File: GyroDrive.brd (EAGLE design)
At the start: 10.7 x 19.8 mm, 42 parts, among them IC1 AD8235, IC2 AD8235, IC3 AD8235, IC4 AD8235

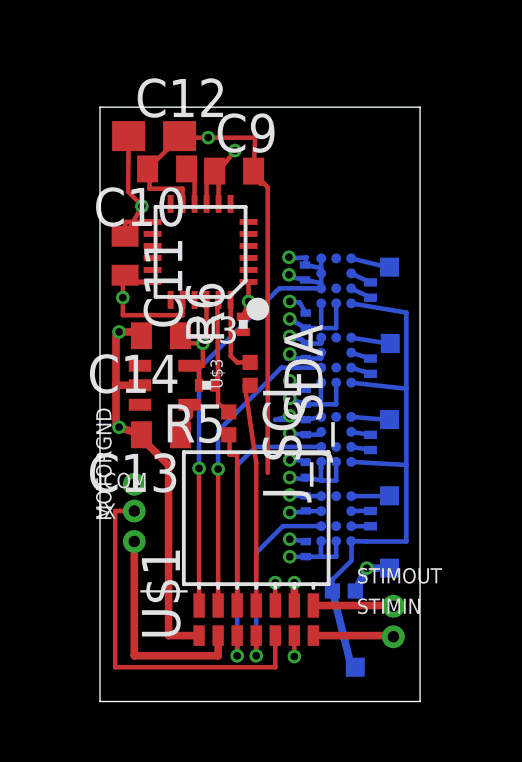
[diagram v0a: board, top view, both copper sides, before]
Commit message: Cleaned up routing around in-amps
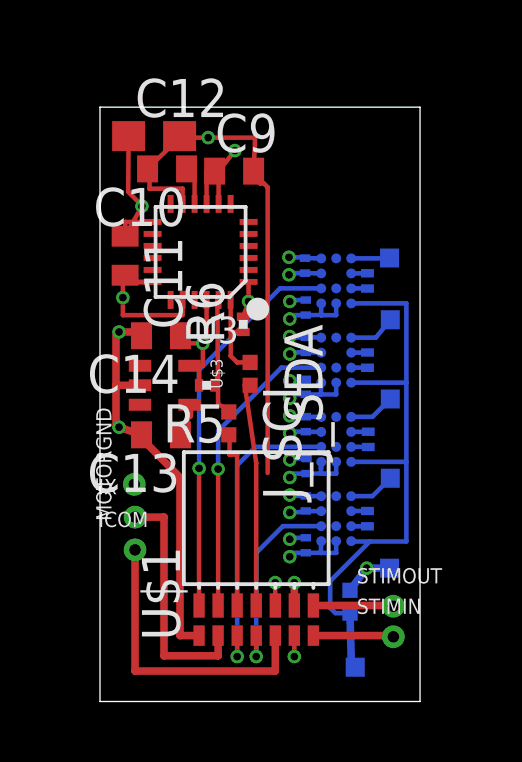
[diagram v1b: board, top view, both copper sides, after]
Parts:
- moved ICOM 1.30 mm to (1.17, 5.05)
- moved IX 0.81 mm to (1.17, 6.15)
- moved E2 0.79 mm to (9.68, 12.7)
- moved E3 0.69 mm to (9.68, 10.1)
- moved E4 0.58 mm to (9.68, 7.44)
- moved C15 0.43 mm to (6.86, 13.1)
- moved J_VGND 0.41 mm to (8.33, 3.33), turned to 90 degrees
- moved C17 0.33 mm to (6.86, 10.5)
- moved R7 0.32 mm to (8.92, 14.0)
- moved E1 0.30 mm to (9.65, 14.8)
- moved C16 0.23 mm to (6.83, 14.5)
- moved R8 0.23 mm to (8.92, 11.4)
- moved C18 0.20 mm to (6.86, 11.9)
- moved C19 0.13 mm to (6.88, 7.85)
- moved R9 0.13 mm to (8.94, 8.74)
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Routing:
- net ICOM: track 12.2 -> 9.89 mm
- net +VS: track 14.1 -> 12.2 mm
- net -VS: track 13.4 -> 11.7 mm
- net VGND: track 19.7 -> 20.7 mm
- net AGND: track 10.6 -> 9.61 mm
- net IX: track 7.28 -> 8.06 mm

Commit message: Switched +VS and -VS on pinout and analog power layer. Finished routing!
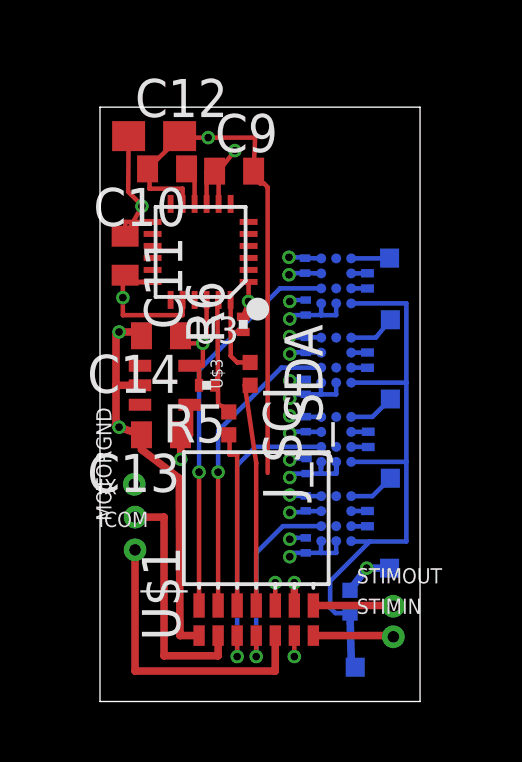
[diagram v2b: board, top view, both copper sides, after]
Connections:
- net +VS: now also U$1.T; no longer U$1.U
- net -VS: now also U$1.U; no longer U$1.T
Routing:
- net +VS: track 12.2 -> 27.2 mm, vias 5 -> 6
- net -VS: track 11.7 -> 5.64 mm
- added copper zone on layer 2, net -VS
- removed copper zone on layer 2, net +VS
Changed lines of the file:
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@@
 <wire x1="6.8152" y1="14.7788" x2="7.374" y2="14.7708" width="0.1524" layer="16"/>
 <wire x1="6.8834" y1="14.8042" x2="6.2992" y2="14.8082" width="0.1524" layer="16"/>
-<contactref element="U$1" pad="T"/>
-<wire x1="5.842" y1="3.2004" x2="5.842" y2="3.9624" width="0.1524" layer="1"/>
-<via x="5.842" y="3.9624" extent="1-16" drill="0.254"/>
-<wire x1="5.842" y1="3.9624" x2="5.842" y2="6.8834" width="0.1524" layer="2"/>
-<wire x1="5.842" y1="6.8834" x2="5.842" y2="9.398" width="0.1524" layer="2"/>
-<wire x1="5.842" y1="9.398" x2="6.3246" y2="9.525" width="0.1524" layer="2"/>
 <wire x1="6.858" y1="6.854" x2="6.354" y2="6.854" width="0.1524" layer="16"/>
 <wire x1="6.354" y1="6.854" x2="6.3246" y2="6.8834" width="0.1524" layer="16"/>
 <via x="6.3246" y="6.8834" extent="1-16" drill="0.254"/>
-<wire x1="6.3246" y1="6.8834" x2="5.842" y2="6.8834" width="0.1524" layer="2"/>
 <wire x1="7.374" y1="9.4876" x2="6.866" y2="9.4876" width="0.1524" layer="16"/>
 <wire x1="6.866" y1="9.4876" x2="6.858" y2="9.4956" width="0.1524" layer="16"/>
 <wire x1="6.858" y1="9.4956" x2="6.354" y2="9.4956" width="0.1524" layer="16"/>
 <wire x1="6.354" y1="9.4956" x2="6.3246" y2="9.525" width="0.1524" layer="16"/>
-<wire x1="7.374" y1="12.1372" x2="7.374" y2="14.7708" width="0" layer="19" extent="16-16"/>
-<wire x1="6.3246" y1="9.525" x2="6.3286" y2="12.1412" width="0" layer="19" extent="16-16"/>
-</signal>
-<signal name="+VS">
 <contactref element="U$1" pad="U"/>
+<wire x1="6.477" y1="3.2004" x2="6.477" y2="3.9624" width="0.254" layer="1"/>
+<via x="6.477" y="3.9624" extent="1-16" drill="0.254"/>
+<wire x1="6.477" y1="3.9624" x2="6.477" y2="4.318" width="0.254" layer="2"/>
 <polygon width="0.1524" layer="2">
 <vertex x="6.223" y="0"/>
 <vertex x="10.541" y="0"/>
-<vertex x="10.541" y="12.954"/>
-<vertex x="6.096" y="13.208"/>
+<vertex x="10.668" y="15.4178"/>
+<vertex x="6.0198" y="15.3924"/>
 </polygon>
+</signal>
+<signal name="+VS">
 <contactref element="U$3" pad="4"/>
 <contactref element="C13" pad="1"/>
-<wire x1="2.984" y1="9.891" x2="2.984" y2="9.525" width="0.254" layer="1"/>
-<wire x1="2.984" y1="9.525" x2="2.682" y2="8.89" width="0.1524" layer="1"/>
 <contactref element="IC1" pad="A1"/>
 <contactref element="IC2" pad="A1"/>
@@
 <wire x1="7.366" y1="5.346" x2="7.374" y2="5.346" width="0.1524" layer="16"/>
 <wire x1="7.874" y1="7.9876" x2="7.874" y2="7.5946" width="0.1524" layer="16"/>
-<wire x1="7.874" y1="7.5946" x2="7.366" y2="7.5946" width="0.1524" layer="16"/>
-<wire x1="7.366" y1="7.5946" x2="7.366" y2="7.759" width="0.1524" layer="16"/>
 <wire x1="7.366" y1="7.759" x2="7.374" y2="7.9876" width="0.1524" layer="16"/>
 <wire x1="7.366" y1="7.759" x2="7.366" y2="7.87" width="0.1524" layer="16"/>
@@
 <wire x1="6.858" y1="12.8818" x2="7.374" y2="12.8818" width="0.1524" layer="16"/>
 <wire x1="7.374" y1="12.8818" x2="7.374" y2="12.8778" width="0.1524" layer="16"/>
-<wire x1="6.8834" y1="7.5986" x2="6.3206" y2="7.5946" width="0.1524" layer="16"/>
-<wire x1="6.3206" y1="7.5946" x2="6.3246" y2="7.4676" width="0.1524" layer="16"/>
 <via x="6.3246" y="7.4676" extent="1-16" drill="0.254"/>
 <wire x1="7.366" y1="7.5946" x2="7.362" y2="7.5986" width="0.1524" layer="16"/>
-<wire x1="7.362" y1="7.5986" x2="6.8834" y2="7.5986" width="0.1524" layer="16"/>
 <wire x1="6.858" y1="4.957" x2="6.3206" y2="4.953" width="0.1524" layer="16"/>
 <wire x1="6.3206" y1="4.953" x2="6.3246" y2="4.826" width="0.1524" layer="16"/>
@@
 <wire x1="7.366" y1="4.953" x2="7.3874" y2="4.957" width="0.1524" layer="16"/>
 <wire x1="7.3874" y1="4.957" x2="6.858" y2="4.957" width="0.1524" layer="16"/>
-<wire x1="6.477" y1="3.2004" x2="6.477" y2="3.9624" width="0.254" layer="1"/>
-<via x="6.477" y="3.9624" extent="1-16" drill="0.254"/>
-<wire x1="6.477" y1="3.9624" x2="6.477" y2="4.318" width="0.254" layer="2"/>
-<wire x1="6.3246" y1="10.1092" x2="2.984" y2="9.891" width="0" layer="19" extent="1-16"/>
+<contactref element="U$1" pad="T"/>
+<wire x1="5.842" y1="3.2004" x2="5.842" y2="3.9624" width="0.1524" layer="1"/>
+<via x="5.842" y="3.9624" extent="1-16" drill="0.254"/>
+<wire x1="5.842" y1="3.9624" x2="5.842" y2="4.826" width="0.1524" layer="2"/>
+<wire x1="5.842" y1="4.826" x2="5.842" y2="7.4676" width="0.1524" layer="2"/>
+<wire x1="5.842" y1="7.4676" x2="5.842" y2="8.0772" width="0.1524" layer="2"/>
+<wire x1="5.842" y1="8.0772" x2="5.842" y2="10.1092" width="0.1524" layer="2"/>
+<wire x1="5.842" y1="10.1092" x2="5.842" y2="12.7508" width="0.1524" layer="2"/>
+<wire x1="5.842" y1="12.7508" x2="6.3246" y2="12.7508" width="0.1524" layer="2"/>
+<wire x1="6.3246" y1="4.826" x2="5.842" y2="4.826" width="0.1524" layer="2"/>
+<wire x1="6.3246" y1="10.1092" x2="5.842" y2="10.1092" width="0.1524" layer="2"/>
+<wire x1="6.3246" y1="7.4676" x2="5.842" y2="7.4676" width="0.1524" layer="2"/>
+<wire x1="7.874" y1="7.9876" x2="7.874" y2="7.5986" width="0.1524" layer="16"/>
+<wire x1="7.874" y1="7.5986" x2="7.366" y2="7.5986" width="0.1524" layer="16"/>
+<wire x1="7.366" y1="7.759" x2="7.366" y2="7.5986" width="0.1524" layer="16"/>
+<wire x1="7.362" y1="7.5986" x2="6.8834" y2="7.5986" width="0.1524" layer="16"/>
+<wire x1="6.8834" y1="7.5986" x2="6.3246" y2="7.5986" width="0.1524" layer="16"/>
+<wire x1="6.3246" y1="7.5986" x2="6.3246" y2="7.4676" width="0.1524" layer="16"/>
+<wire x1="2.682" y1="8.89" x2="2.6924" y2="8.89" width="0.1524" layer="1"/>
+<wire x1="2.6924" y1="8.89" x2="2.6924" y2="8.0772" width="0.254" layer="1"/>
+<via x="2.6924" y="8.0772" extent="1-16" drill="0.254"/>
+<wire x1="2.6924" y1="8.0772" x2="5.842" y2="8.0772" width="0.1524" layer="2"/>
+<wire x1="2.984" y1="9.891" x2="2.984" y2="8.89" width="0.254" layer="1"/>
+<wire x1="2.984" y1="8.89" x2="2.682" y2="8.89" width="0.254" layer="1"/>
+<wire x1="7.366" y1="7.5986" x2="7.362" y2="7.5986" width="0.1524" layer="16"/>
 </signal>
 <signal name="AGND">
@@
 <contactref element="IC1" pad="B1"/>
 <contactref element="U$1" pad="E"/>
-<wire x1="3.302" y1="3.2004" x2="3.302" y2="7.7724" width="0.1524" layer="1"/>
+<wire x1="3.302" y1="3.2004" x2="3.302" y2="7.6454" width="0.1524" layer="1"/>
 <wire x1="7.374" y1="13.7708" x2="5.9984" y2="13.7708" width="0.1524" layer="16"/>
-<via x="3.302" y="7.7724" extent="1-16" drill="0.254"/>
-<wire x1="3.302" y1="7.7724" x2="3.302" y2="11.049" width="0.1524" layer="16"/>
+<via x="3.302" y="7.6454" extent="1-16" drill="0.254"/>
+<wire x1="3.302" y1="7.6454" x2="3.302" y2="11.049" width="0.1524" layer="16"/>
 <wire x1="3.302" y1="11.049" x2="5.9984" y2="13.7708" width="0.1524" layer="16"/>
 </signal>
@@
 <wire x1="7.374" y1="11.1292" x2="6.0492" y2="11.1292" width="0.1524" layer="16"/>
 <wire x1="6.0492" y1="11.1292" x2="3.937" y2="9.017" width="0.1524" layer="16"/>
-<wire x1="3.937" y1="9.017" x2="3.937" y2="7.747" width="0.1524" layer="16"/>
-<via x="3.937" y="7.747" extent="1-16" drill="0.254"/>
-<wire x1="3.937" y1="7.747" x2="3.937" y2="3.2004" width="0.1524" layer="1"/>
+<wire x1="3.937" y1="9.017" x2="3.937" y2="7.6454" width="0.1524" layer="16"/>
+<via x="3.937" y="7.6454" extent="1-16" drill="0.254"/>
+<wire x1="3.937" y1="7.6454" x2="3.937" y2="3.2004" width="0.1524" layer="1"/>
 </signal>
 <signal name="VGND">
@@
 <polygon width="0.1524" layer="2">
 <vertex x="0" y="19.812"/>
-<vertex x="0" y="8.382"/>
-<vertex x="5.588" y="8.382"/>
+<vertex x="0" y="-0.0254"/>
+<vertex x="5.7404" y="0"/>
 <vertex x="5.588" y="19.812"/>
 </polygon>
@@
 <contactref element="U$1" pad="A"/>
 <wire x1="3.302" y1="2.1971" x2="2.667" y2="2.1971" width="0.254" layer="1"/>
-<wire x1="2.667" y1="2.1971" x2="2.667" y2="7.4676" width="0.254" layer="1"/>
-<wire x1="2.667" y1="7.4676" x2="1.382" y2="8.778" width="0.254" layer="1"/>
-<wire x1="1.382" y1="8.778" x2="1.382" y2="8.89" width="0.254" layer="1"/>
+<wire x1="2.667" y1="2.1971" x2="2.6416" y2="7.4422" width="0.254" layer="1"/>
+<wire x1="2.6416" y1="7.4422" x2="1.382" y2="8.397" width="0.254" layer="1"/>
+<wire x1="1.382" y1="8.397" x2="1.382" y2="8.89" width="0.254" layer="1"/>
 </signal>
 <signal name="SDA">

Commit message: Added bypass capacitor for SDA pull-up resistor, shorted SDA and SCL jumpers with traces
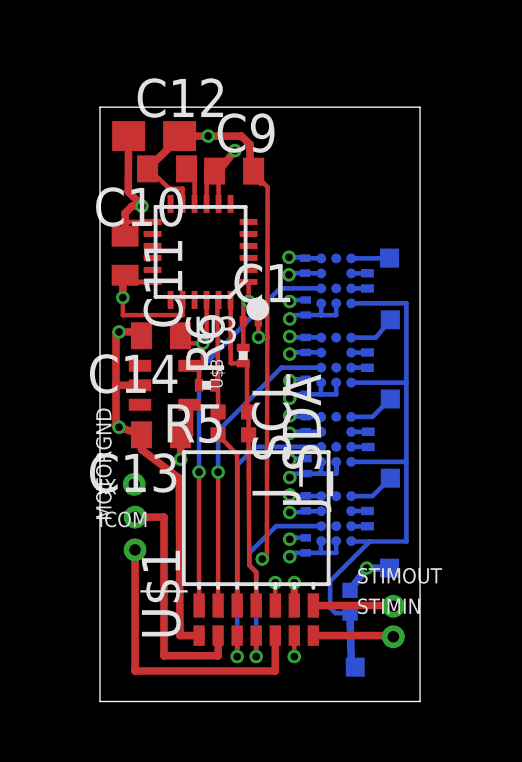
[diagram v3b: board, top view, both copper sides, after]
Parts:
- added C1: (no value), resistor:C0201
- moved J_SDA 1.65 mm to (4.95, 9.27)
- moved R6 1.04 mm to (4.78, 11.5)
- moved J_SCL 0.36 mm to (3.94, 9.27)
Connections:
- net DGND: now also C1.2
- net VDD: now also C1.1
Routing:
- net DGND: track 38.1 -> 42.7 mm, vias 4 -> 6
- net SDAOUT: track 7.55 -> 5.78 mm
- net VDD: track 26.2 -> 27.6 mm
- net SDA: track 3.02 -> 4.43 mm

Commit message: Changed pinout to group digital signals closer together
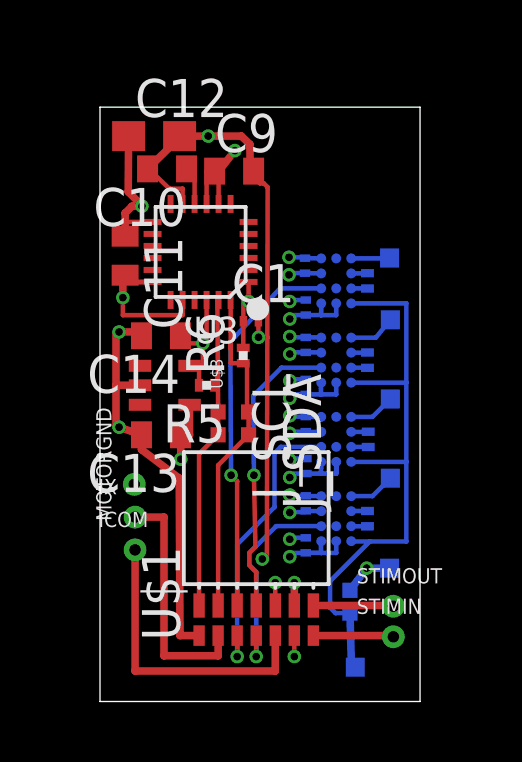
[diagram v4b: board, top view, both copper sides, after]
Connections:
- net S1: now also U$1.R; no longer U$1.E
- net S2: now also U$1.L; no longer U$1.N
- net SCLOUT: now also U$1.E; no longer U$1.R
- net SDAOUT: now also U$1.N; no longer U$1.L
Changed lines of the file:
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@@
 <layers>
 <layer number="1" name="Top" color="4" fill="1" visible="yes" active="yes"/>
-<layer number="2" name="Route2" color="13" fill="3" visible="no" active="yes"/>
+<layer number="2" name="Route2" color="13" fill="3" visible="yes" active="yes"/>
 <layer number="3" name="Route3" color="4" fill="3" visible="no" active="no"/>
 <layer number="14" name="Route14" color="1" fill="6" visible="no" active="no"/>
-<layer number="15" name="Route15" color="11" fill="6" visible="no" active="yes"/>
+<layer number="15" name="Route15" color="11" fill="6" visible="yes" active="yes"/>
 <layer number="16" name="Bottom" color="1" fill="1" visible="yes" active="yes"/>
 <layer number="17" name="Pads" color="2" fill="1" visible="yes" active="yes"/>
@@
 <layer number="20" name="Dimension" color="15" fill="1" visible="yes" active="yes"/>
 <layer number="21" name="tPlace" color="7" fill="1" visible="yes" active="yes"/>
-<layer number="22" name="bPlace" color="7" fill="1" visible="no" active="yes"/>
+<layer number="22" name="bPlace" color="7" fill="1" visible="yes" active="yes"/>
 <layer number="23" name="tOrigins" color="15" fill="1" visible="yes" active="yes"/>
 <layer number="24" name="bOrigins" color="15" fill="1" visible="yes" active="yes"/>
@@
 <signal name="S1">
 <contactref element="IC1" pad="B1"/>
-<contactref element="U$1" pad="E"/>
-<wire x1="3.302" y1="3.2004" x2="3.302" y2="7.6454" width="0.1524" layer="1"/>
 <wire x1="7.374" y1="13.7708" x2="5.9984" y2="13.7708" width="0.1524" layer="16"/>
-<via x="3.302" y="7.6454" extent="1-16" drill="0.254"/>
-<wire x1="3.302" y1="7.6454" x2="3.302" y2="11.049" width="0.1524" layer="16"/>
-<wire x1="3.302" y1="11.049" x2="5.9984" y2="13.7708" width="0.1524" layer="16"/>
+<via x="4.3688" y="7.5438" extent="1-16" drill="0.254"/>
+<wire x1="4.3688" y1="7.5438" x2="4.3434" y2="11.9888" width="0.1524" layer="16"/>
+<wire x1="4.3434" y1="11.9888" x2="5.9984" y2="13.7708" width="0.1524" layer="16"/>
+<contactref element="U$1" pad="R"/>
+<wire x1="4.3688" y1="7.5438" x2="4.572" y2="7.3406" width="0.1524" layer="1"/>
+<wire x1="4.572" y1="7.3406" x2="4.572" y2="3.2004" width="0.1524" layer="1"/>
 </signal>
 <signal name="S2">
 <contactref element="IC2" pad="B1"/>
-<contactref element="U$1" pad="N"/>
 <wire x1="7.374" y1="11.1292" x2="6.0492" y2="11.1292" width="0.1524" layer="16"/>
-<wire x1="6.0492" y1="11.1292" x2="3.937" y2="9.017" width="0.1524" layer="16"/>
-<wire x1="3.937" y1="9.017" x2="3.937" y2="7.6454" width="0.1524" layer="16"/>
-<via x="3.937" y="7.6454" extent="1-16" drill="0.254"/>
-<wire x1="3.937" y1="7.6454" x2="3.937" y2="3.2004" width="0.1524" layer="1"/>
+<wire x1="6.0492" y1="11.1292" x2="5.1054" y2="10.1854" width="0.1524" layer="16"/>
+<wire x1="5.1054" y1="10.1854" x2="5.1308" y2="7.5438" width="0.1524" layer="16"/>
+<via x="5.1308" y="7.5438" extent="1-16" drill="0.254"/>
+<contactref element="U$1" pad="L"/>
+<wire x1="5.1308" y1="7.5438" x2="5.1816" y2="5.1562" width="0.1524" layer="1"/>
+<wire x1="5.1816" y1="5.1562" x2="4.9784" y2="4.953" width="0.1524" layer="1"/>
+<wire x1="4.9784" y1="4.953" x2="4.9784" y2="4.5466" width="0.1524" layer="1"/>
+<wire x1="4.9784" y1="4.5466" x2="5.207" y2="4.318" width="0.1524" layer="1"/>
+<wire x1="5.207" y1="4.318" x2="5.207" y2="3.2004" width="0.1524" layer="1"/>
 </signal>
 <signal name="VGND">
@@
 <contactref element="IC3" pad="B1"/>
 <contactref element="U$1" pad="F"/>
-<wire x1="7.374" y1="8.4876" x2="5.1856" y2="8.4876" width="0.1524" layer="16"/>
-<wire x1="5.1856" y1="8.4876" x2="4.572" y2="7.874" width="0.1524" layer="16"/>
-<wire x1="4.572" y1="7.874" x2="4.572" y2="1.4986" width="0.1524" layer="16"/>
 <via x="4.572" y="1.4986" extent="1-16" drill="0.254"/>
 <wire x1="4.572" y1="1.4986" x2="4.572" y2="2.1971" width="0.1524" layer="1"/>
+<wire x1="7.374" y1="8.4876" x2="6.0238" y2="8.4876" width="0.1524" layer="16"/>
+<wire x1="6.0238" y1="8.4876" x2="5.8166" y2="8.2804" width="0.1524" layer="16"/>
+<wire x1="5.8166" y1="8.2804" x2="5.8166" y2="6.477" width="0.1524" layer="16"/>
+<wire x1="5.8166" y1="6.477" x2="4.572" y2="5.2324" width="0.1524" layer="16"/>
+<wire x1="4.572" y1="5.2324" x2="4.572" y2="1.4986" width="0.1524" layer="16"/>
 </signal>
 <signal name="S4">
@@
 <signal name="SDAOUT">
 <contactref element="J_SDA" pad="2"/>
-<contactref element="U$1" pad="L"/>
-<wire x1="4.953" y1="8.4074" x2="4.9784" y2="4.5466" width="0.1524" layer="1"/>
-<wire x1="4.9784" y1="4.5466" x2="5.207" y2="4.318" width="0.1524" layer="1"/>
-<wire x1="5.207" y1="4.318" x2="5.207" y2="3.2004" width="0.1524" layer="1"/>
-<wire x1="4.953" y1="8.4074" x2="4.953" y2="8.89" width="0.1524" layer="1"/>
+<contactref element="U$1" pad="N"/>
+<wire x1="4.953" y1="8.89" x2="3.937" y2="7.874" width="0.1524" layer="1"/>
+<wire x1="3.937" y1="7.874" x2="3.937" y2="3.2004" width="0.1524" layer="1"/>
 </signal>
 <signal name="SCLOUT">
 <contactref element="J_SCL" pad="2"/>
-<wire x1="4.572" y1="8.2296" x2="3.937" y2="8.89" width="0.1524" layer="1"/>
-<contactref element="U$1" pad="R"/>
-<wire x1="4.572" y1="8.2296" x2="4.572" y2="3.2004" width="0.1524" layer="1"/>
+<contactref element="U$1" pad="E"/>
+<wire x1="3.937" y1="8.89" x2="3.302" y2="8.255" width="0.1524" layer="1"/>
+<wire x1="3.302" y1="8.255" x2="3.302" y2="3.2004" width="0.1524" layer="1"/>
 </signal>
 <signal name="IX">

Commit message: Added high pass filters in front of inputs to in-amps
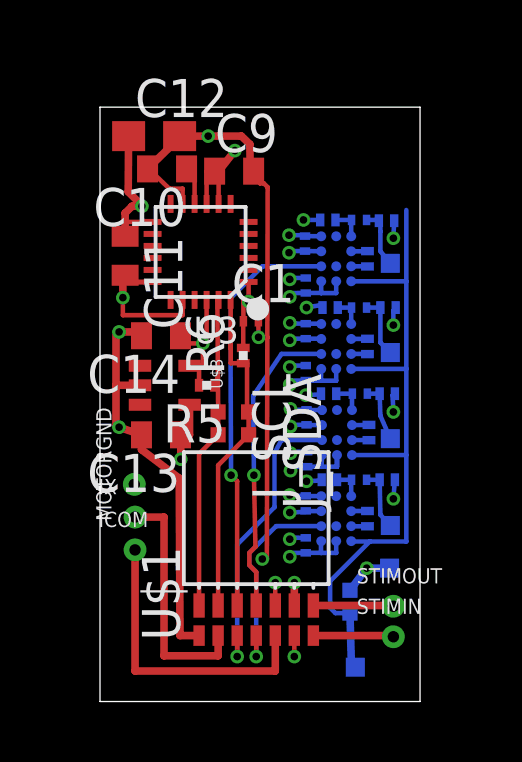
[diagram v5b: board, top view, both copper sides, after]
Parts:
- added C2, C3, C4, C5: (no value), resistor:C0201
- added R1, R11, R12, R13, R14, R2, R3, R4: (no value), resistor:R0201
- moved E4 1.57 mm to (9.68, 5.87)
- moved E3 1.32 mm to (9.68, 8.76)
- moved E2 1.09 mm to (9.68, 11.6)
- moved IC1 0.74 mm to (7.87, 14.8)
- moved R7 0.74 mm to (8.92, 14.8)
- moved C15 0.74 mm to (6.86, 13.9)
- moved C16 0.74 mm to (6.83, 15.3)
- moved C17 0.46 mm to (6.86, 10.9)
- moved C18 0.46 mm to (6.86, 12.3)
- moved IC2 0.46 mm to (7.87, 11.8)
- moved R8 0.46 mm to (8.92, 11.8)
- moved R9 0.23 mm to (8.97, 8.97)
- moved C20 0.23 mm to (6.88, 9.47)
- moved IC3 0.23 mm to (7.90, 8.97)
- moved C19 0.23 mm to (6.91, 8.08)
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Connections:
- new net N$4: C4.2, IC3.D3, R12.2
- new net N$6: C2.2, IC1.D3, R2.2
- new net N$8: C5.2, IC4.D3, R14.2
- new net N$9: C3.2, IC2.D3, R4.2
- net AGND: now also R1.1, R11.1, R12.1, R13.1, R14.1, R2.1, R3.1, R4.1
- net E1: now also C2.1, R1.2; no longer IC1.D3
- net E2: now also C3.1, R3.2; no longer IC2.D3
- net E3: now also C4.1, R11.2; no longer IC3.D3
- net E4: now also C5.1, R13.2; no longer IC4.D3
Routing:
- net AGND: track 9.61 -> 14.2 mm, vias 10 -> 18
- net VGND: track 20.7 -> 23.8 mm
- net S1: track 12.7 -> 13.8 mm
- net N$4: track 0.00 -> 1.09 mm
- net N$6: track 0.00 -> 1.08 mm
- net N$8: track 0.00 -> 1.04 mm
- net N$9: track 0.00 -> 1.01 mm
- net E1: track 1.28 -> 2.01 mm
- net +VS: track 27.2 -> 27.8 mm
- net E4: track 1.55 -> 2.09 mm
- net E2: track 1.59 -> 2.10 mm
